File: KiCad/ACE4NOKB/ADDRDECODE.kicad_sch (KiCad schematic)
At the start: 7 parts

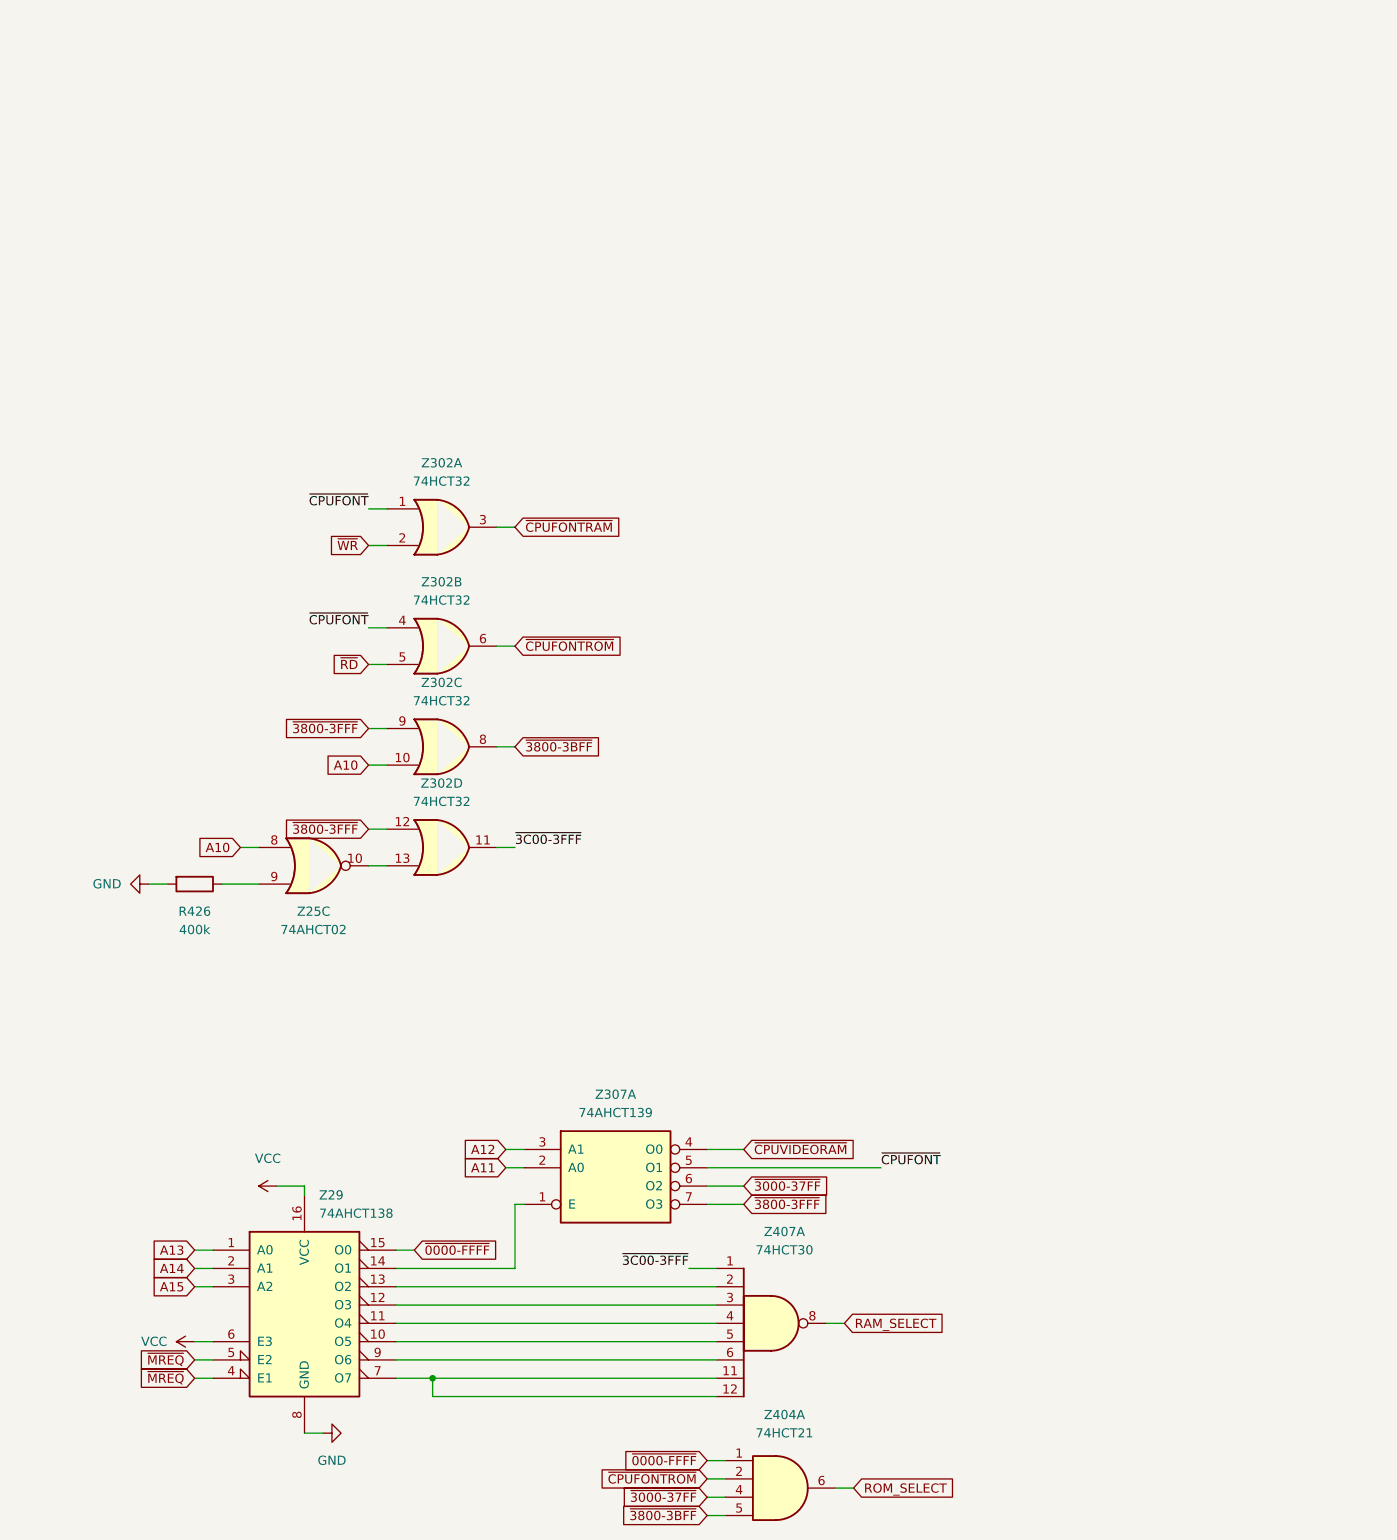
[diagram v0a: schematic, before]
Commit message: Fix mistake with ROM Select.
Signed-off-by: John Bradley <flypie@rocketmail.com>
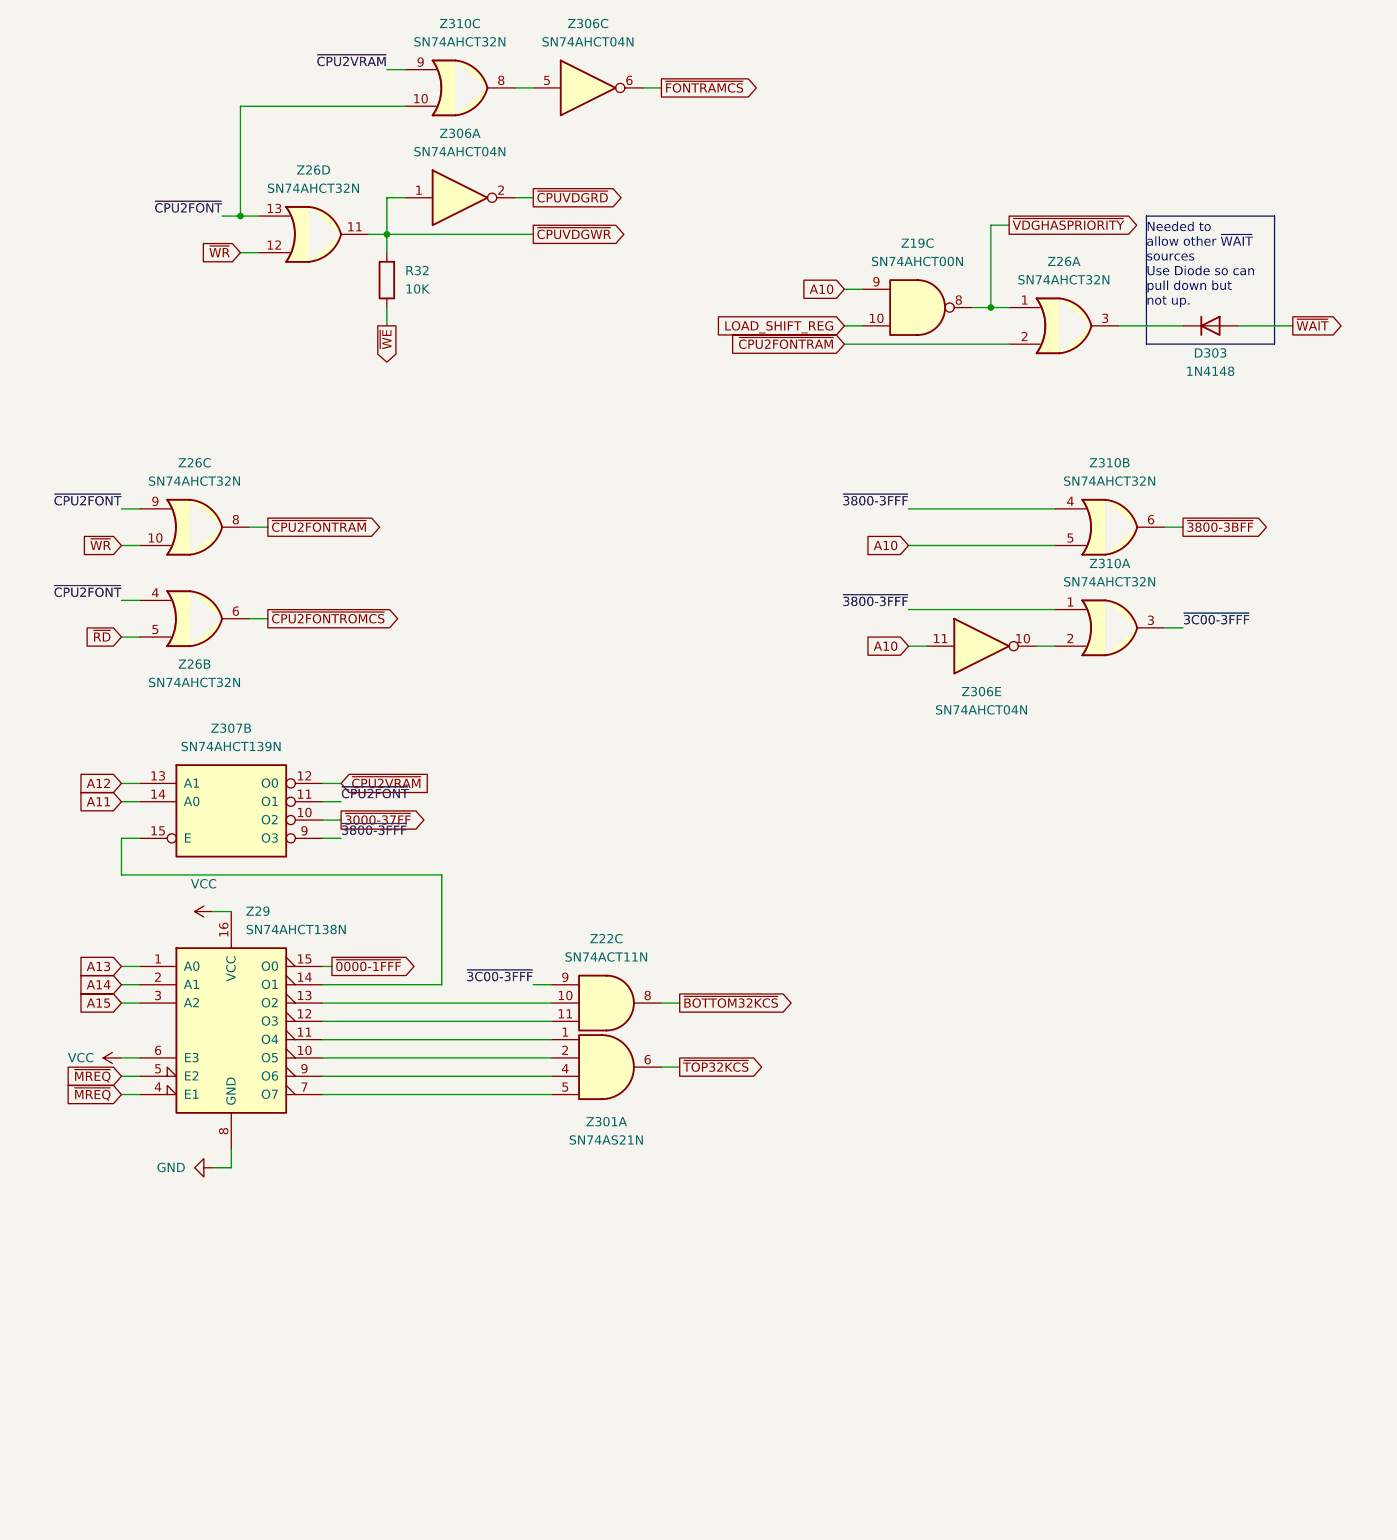
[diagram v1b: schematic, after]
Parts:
- removed R426: 400k, Resistor_THT:R_Axial_DIN0204_L3.6mm_D1.6mm_P1.90mm_Vertical, symbol Device:R
- removed Z25: 74AHCT02, Package_DIP:DIP-14_W7.62mm_Socket, symbol 74xx:74LS02
- removed Z302: 74HCT32, Package_DIP:DIP-14_W7.62mm_Socket, symbol 74xx:74LS32
- removed Z307: 74AHCT139, Package_DIP:DIP-16_W7.62mm_Socket, symbol 74xx:74LS139
- removed Z404: 74HCT21, Package_DIP:DIP-14_W7.62mm_Socket, symbol 74xx:74LS21
- removed Z407: 74HCT30, Package_DIP:DIP-14_W7.62mm_Socket, symbol 74xx:74LS30
- added D303: 1N4148, Diode_THT:D_DO-35_SOD27_P2.54mm_Vertical_AnodeUp, symbol Diode:1N4148
- added R32: 10K, Resistor_THT:R_Axial_DIN0204_L3.6mm_D1.6mm_P1.90mm_Vertical, symbol Device:R
- added Z19: SN74AHCT00N, Package_DIP:DIP-14_W7.62mm, symbol 74xx:74LS00
- added Z22: SN74ACT11N, Package_DIP:DIP-14_W7.62mm, symbol 74xx:74LS11
- added Z26, Z310: SN74AHCT32N, Package_DIP:DIP-14_W7.62mm, symbol 74xx:74LS32
- added Z301: SN74AS21N, Package_DIP:DIP-14_W7.62mm, symbol 74xx-FIX:74LS21
- added Z306: SN74AHCT04N, Package_DIP:DIP-14_W7.62mm, symbol 74xx:74LS04
- added Z307: SN74AHCT139N, Package_DIP:DIP-16_W7.62mm, symbol 74xx:74LS139
- Z29: value 74AHCT138 -> SN74AHCT138N; footprint Package_DIP:DIP-16_W7.62mm_Socket -> Package_DIP:DIP-16_W7.62mm
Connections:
- net A10: now also Z19.9, Z306.11, Z310.5
- net A11: now also Z307.14 (A0)
- net A12: now also Z307.13 (A1)
- net ~{3000-37FF}: now also Z307.10 (O2)
- net ~{3800-3BFF}: now also Z310.6
- net ~{3800-3FFF}: now also Z307.9 (O3), Z310.1, Z310.4
- net ~{3C00-3FFF}: now also Z22.9, Z310.3
- net ~{RD}: now also Z26.5
- net ~{WR}: now also Z26.10, Z26.12
- net at Z29.14 (O1): now also Z307.15 (E)
- net at Z29.7 (O7): now also Z301.5
- net at Z29.13 (O2): now also Z22.10
- net at Z29.12 (O3): now also Z22.11
- net at Z29.11 (O4): now also Z301.1
- net at Z29.10 (O5): now also Z301.2
- net at Z29.9 (O6): now also Z301.4
- net ~{0000-FFFF} renamed ~{0000-1FFF}
- new net: D303.1 (K), Z26.3
- new net: Z306.5, Z310.8
- new net: Z306.10, Z310.2
- new net LOAD_SHIFT_REG: Z19.10
- new net ~{BOTTOM32KCS}: Z22.8
- new net ~{CPU2FONTRAM}: Z26.2, Z26.8
- new net ~{CPU2FONTROMCS}: Z26.6
- new net ~{CPU2FONT}: Z26.13, Z26.4, Z26.9, Z307.11 (O1), Z310.10
- new net ~{CPU2VRAM}: Z307.12 (O0), Z310.9
- new net ~{CPUVDGRD}: Z306.2
- new net ~{CPUVDGWR}: R32.2, Z26.11, Z306.1
- new net ~{FONTRAMCS}: Z306.6
- new net ~{TOP32KCS}: Z301.6
- new net ~{VDGHASPRIORITY}: Z19.8, Z26.1
- new net ~{WAIT}: D303.2 (A)
- new net ~{WE}: R32.1
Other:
- note added: "Needed to allow other ~{WAIT} sources Use Diode so can pull down but not up."
- title: ACE4NOKB -> JupiterAce Z80 plus KIO and new memory format.
- moved on the sheet: Z29

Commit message: Update to last expermintal version. Uses clock sythsiser and can be switched between full ACE compatible and inhanced IO. Should be able to switch between multiple ROM images tosred on the same chip.
Signed-off-by: John Bradley <flypie@rocketmail.com>
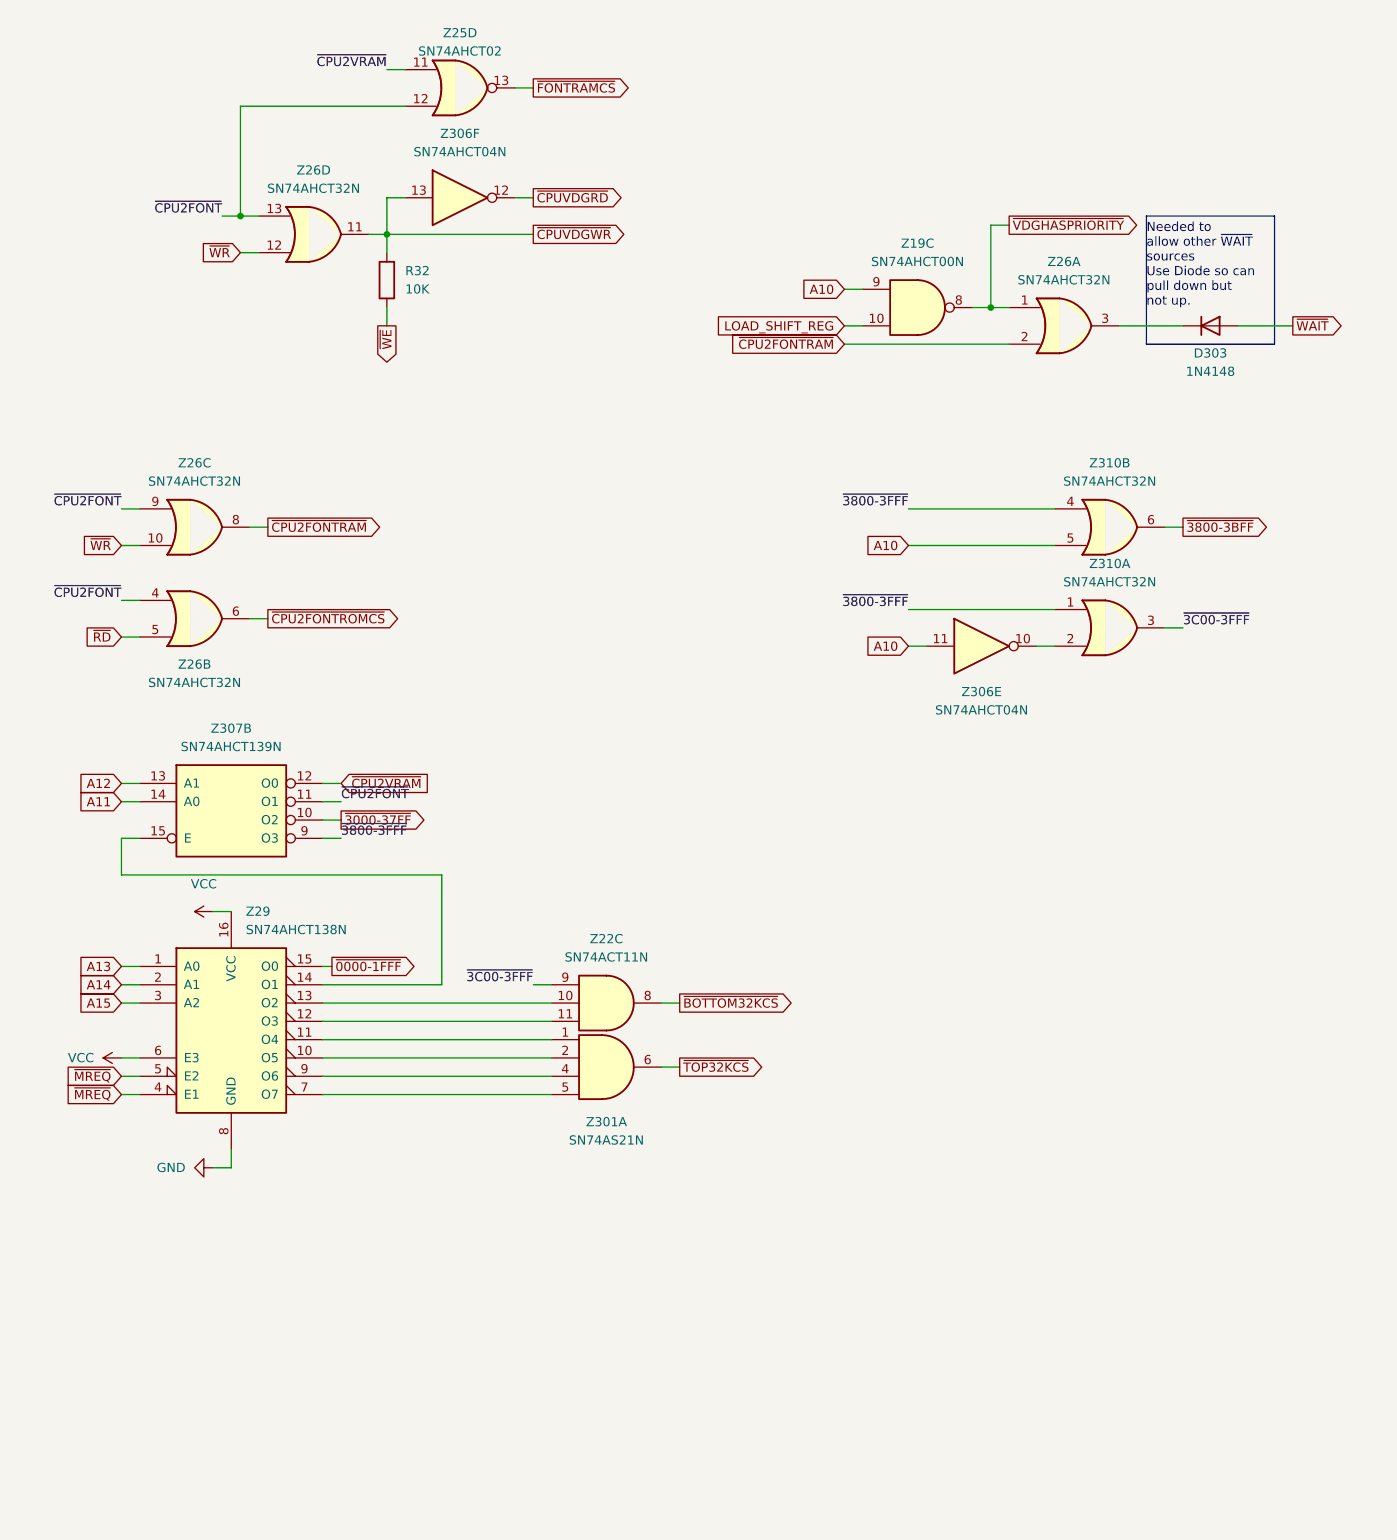
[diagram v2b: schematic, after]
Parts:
- removed unit 3 of Z306
- removed unit 3 of Z310
- added Z25: SN74AHCT02, Package_DIP:DIP-14_W7.62mm, symbol 74xx:74LS02
- Z29: Manufacturer_Name Texas Instruments -> (none); Manufacturer_Part_Number SN74AHCT138N -> (none)
- Z307: Manufacturer_Name Texas Instruments -> (none); Manufacturer_Part_Number SN74AHCT139N -> (none)
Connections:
- net ~{CPU2FONT}: now also Z25.12
- net ~{CPU2VRAM}: now also Z25.11
- net ~{CPUVDGRD}: now also Z306.12; no longer Z306.2
- net ~{CPUVDGWR}: now also Z306.13; no longer Z306.1
- net ~{FONTRAMCS}: now also Z25.13

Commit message: Version with KIO replaced with Z84C15 and Video and Character RAM as MultiPorted.
Signed-off-by: John Bradley <flypie@rocketmail.com>
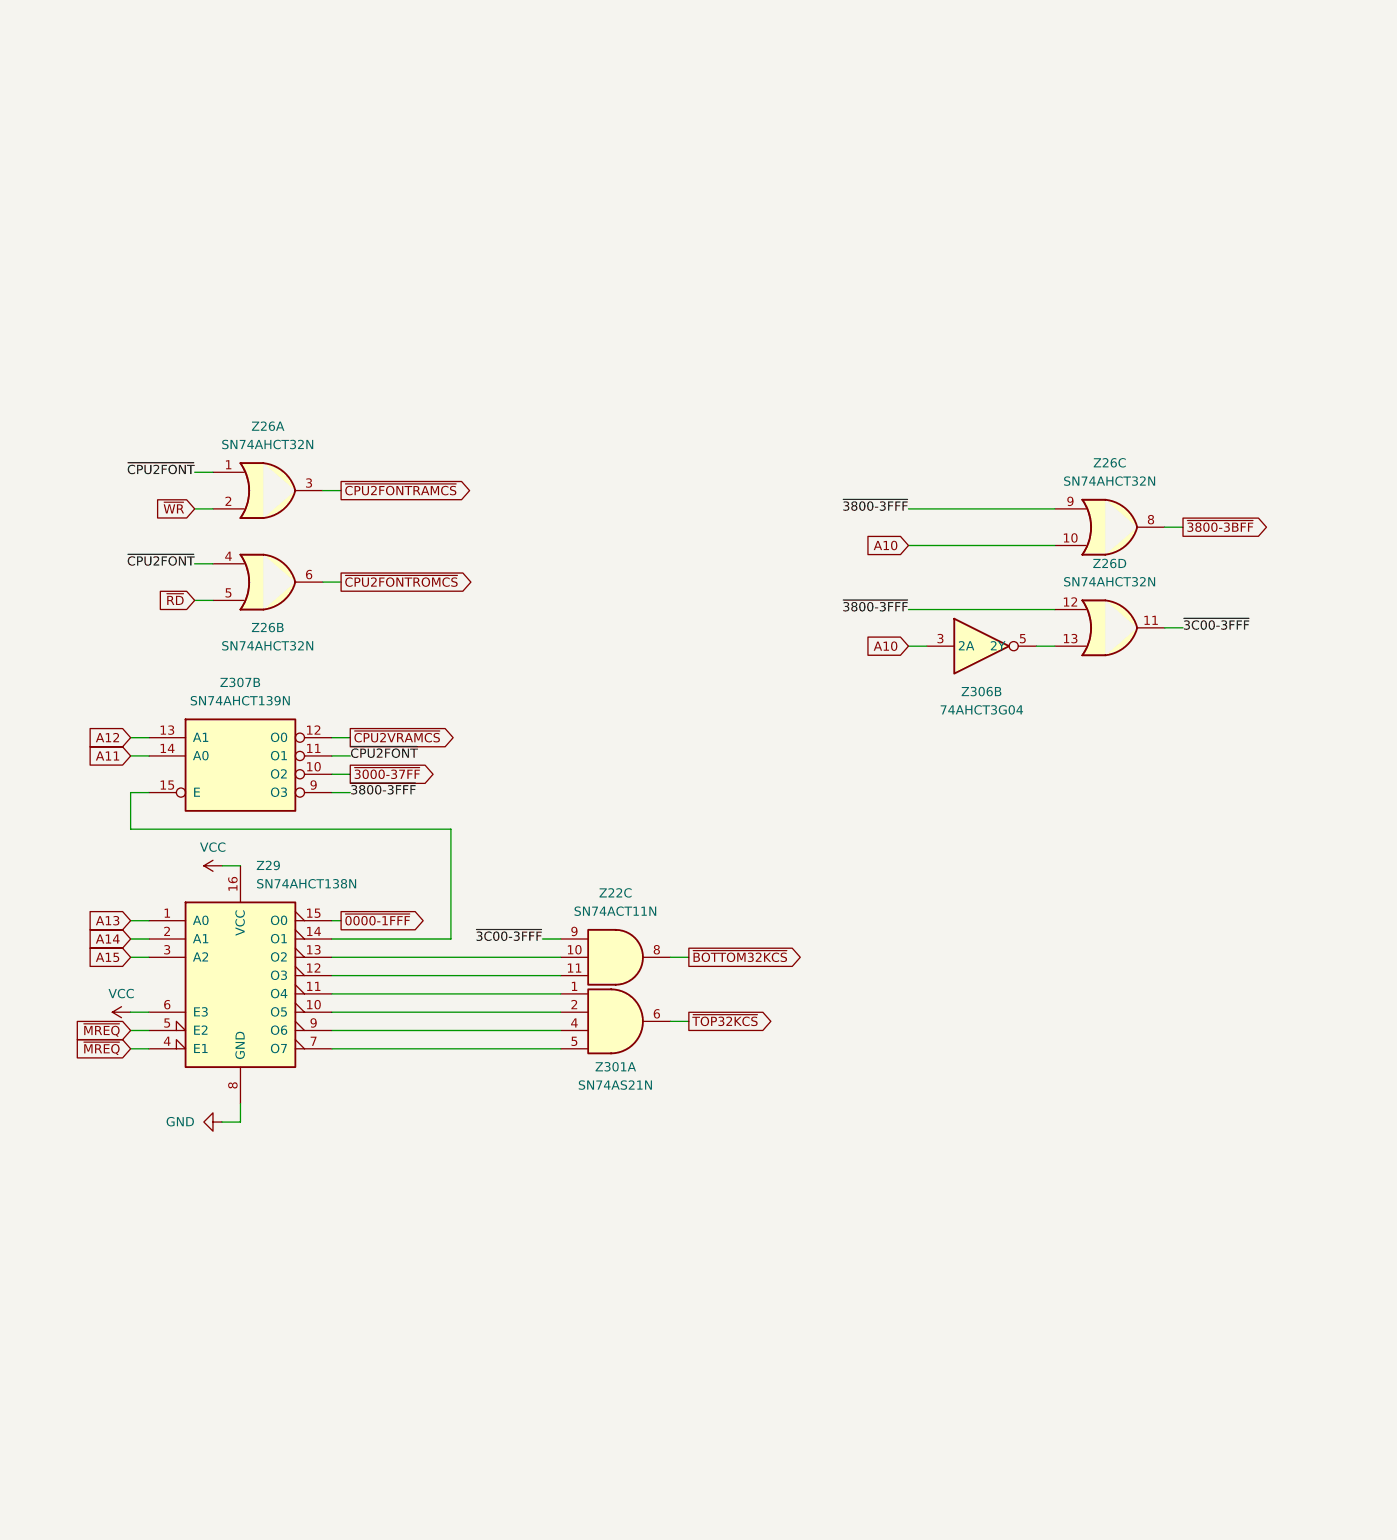
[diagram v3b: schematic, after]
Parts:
- removed D303: 1N4148, Diode_THT:D_DO-35_SOD27_P2.54mm_Vertical_AnodeUp, symbol Diode:1N4148
- removed R32: 10K, Resistor_THT:R_Axial_DIN0204_L3.6mm_D1.6mm_P1.90mm_Vertical, symbol Device:R
- removed Z19: SN74AHCT00N, Package_DIP:DIP-14_W7.62mm, symbol 74xx:74LS00
- removed Z25: SN74AHCT02, Package_DIP:DIP-14_W7.62mm, symbol 74xx:74LS02
- removed unit 1 of Z26
- removed unit 4 of Z26
- removed unit 6 of Z306
- Z306: value SN74AHCT04N -> 74AHCT3G04; footprint Package_DIP:DIP-14_W7.62mm -> Package_SO:TSSOP-8_3x3mm_P0.65mm; symbol 74xx:74LS04 -> ExtraSymbols:74AHCT3G04
- renumbered Z310 to Z26
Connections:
- net A10: now also Z26.10, Z306.3 (2A); no longer Z26.5, Z306.11
- net ~{3800-3BFF}: now also Z26.8; no longer Z26.6
- net ~{3800-3FFF}: now also Z26.12, Z26.9; no longer Z26.1, Z26.4
- net ~{3C00-3FFF}: now also Z26.11; no longer Z26.3
- net ~{CPU2FONT}: now also Z26.1; no longer Z26.9
- net ~{WR}: now also Z26.2; no longer Z26.10
- removed net ~{CPU2FONTRAM}: Z26.8
- net ~{CPU2VRAM} renamed ~{CPU2VRAMCS}
- new net: Z26.13, Z306.5 (2Y)
- new net ~{CPU2FONTRAMCS}: Z26.3
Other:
- note removed: "Needed to allow other ~{WAIT} sources Use Diode so can pull down but not up."
- moved on the sheet: Z22C, Z26A, Z26B, Z29, Z301A, Z307B
